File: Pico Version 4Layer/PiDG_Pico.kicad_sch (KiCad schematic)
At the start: 76 parts, among them J1 Conn_02x05_Odd_Even, J10 Trig, J11 Laser Enable, J12 Pixel Reset, J14 Pico Socket A, J15 Pico Socket B, J16 Laser En/PWM Trig/GND, J17 USB-C PD in, J2 Conn_02x05_Odd_Even, J3 Conn_02x05_Odd_Even, J4 Conn_02x05_Odd_Even, J5 Conn_02x05_Odd_Even, J6 Conn_02x05_Odd_Even, J7 Laser 1, J8 Laser 2, U1 74LVC1G04, U10 74AHCT1G08, U11 Raspberry Pi Pico 2 W, U12 74LVC1G17, U13 UCC27524, U14 CH224K, U15 AP63205WU, U16 LM66100, U17 LT3065EDD, U18 TPS3700DDC, U2 SN74LVC04AD, U3 74LVC1G04, U4 SN74LVC04AD, U5 74LVC1G04, U6 SN74LVC04AD, U7 74AHCT1G08, U8 74AHCT1G08, U9 NCP718xSN180

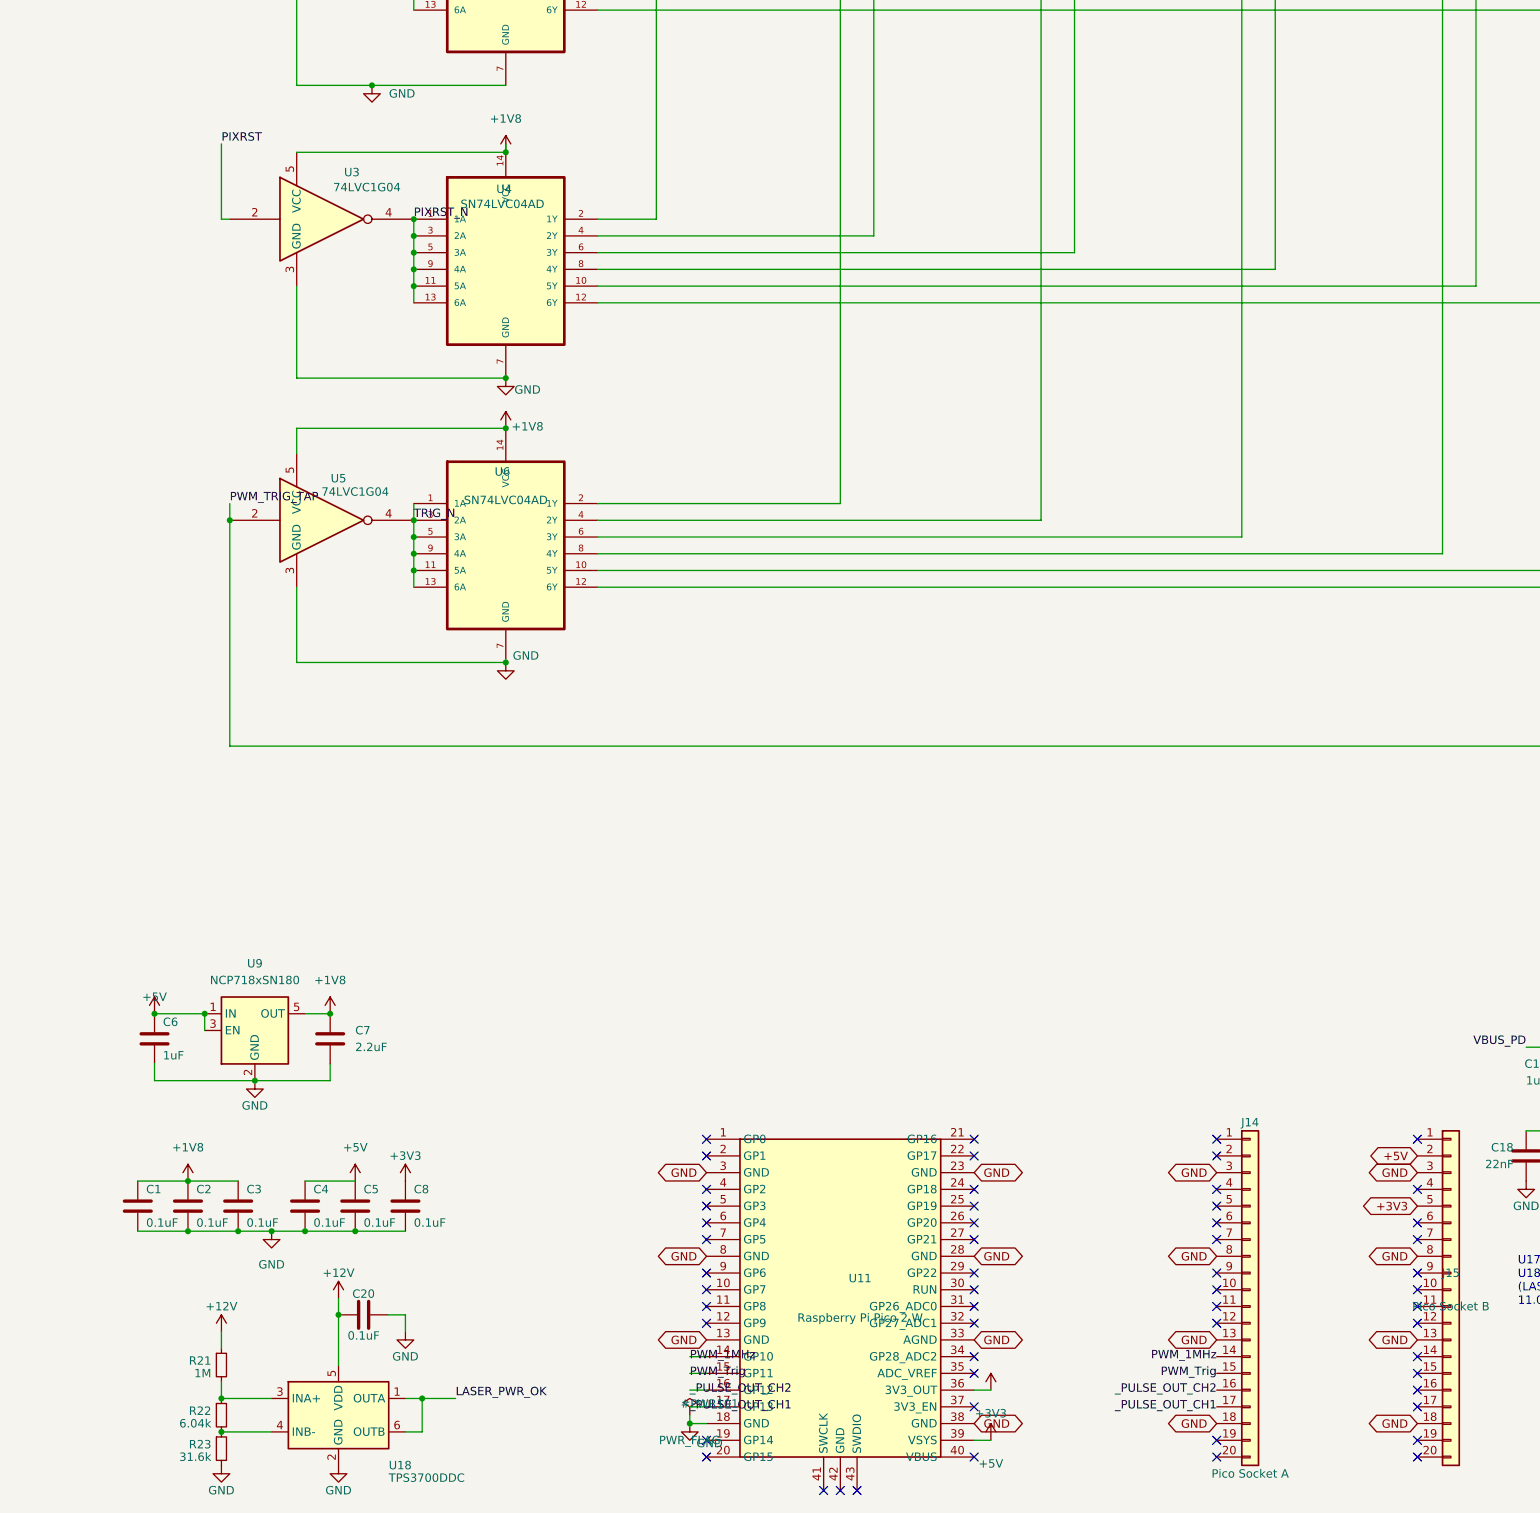
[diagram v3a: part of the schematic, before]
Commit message: Pixel-reset gate: optional camera pixel reset between pulse pairs
The Pico can now hold every camera's pixels in reset (TDRSTN low)
between pulse pairs, like a shutter, while the J12 BNC input keeps
working exactly as before.

Board
- U3 74LVC1G04 -> 74LVC1G00 (NAND, same SOT-23-5 footprint): through U4
  the cameras get TDRSTN = J12 input AND PIXRST_GATE, so either source
  resets the pixels.
- PIXRST_GATE = Pico GP16 (J15 pad 20) -> U3 pin 1 (previously NC), with
  R24 10k pull-up to +3V3 so the gate reads "no reset" unless driven low.
  Routed F.Cu from J15 pad 20, one B.Cu 45-degree hop, into U3 pad 1.
- ERC 0, DRC 0 / 0 unconnected, no real parity net conflicts; gerbers,
  drill, zip, CPLs and BOMs regenerated (U3 = SN74LVC1G00DBVR C7826;
  R24 joins the 10k line). 76 parts, 41 JLC lines.

Firmware
- PIXGATE 0|1|2 (off / while ARMED / always), PIXLEAD ns (pixels
  released this long before CH1, >= 5 cycles), PIXLAG ns (reset again
  this long after the last laser pulse). Validated on realized cycles:
  PIXLEAD + DELAY + WIDTH + PIXLAG <= 1/FREQ - 3 cycles.
- pio0 SM3 runs the existing pulse program on GP16 with the pad output
  inverted (GPIO_OVERRIDE_INVERT), enabled on the same cycle as CH1/CH2/
  MARKER; a stopped gate leaves the pixels free. SYNC moved to pio1 to
  free SM3 (the Pico 2 W's CYW43 driver takes pio2).
- STATUS reports PIXRESET (reset length per period, its start after CH1,
  and the free window); HELP documents the commands.
- tools/timing_check/check_pixgate.py: 1600 random sets against an
  exact model plus a cycle-level PIO simulation of CH1/CH2/gate
  (513 gated, 0 mismatches; mutation-tested). All existing checks give
  their unchanged expected counts. Strict-warning builds clean.

Docs: README (commands, PIXGATE section, STATUS, troubleshooting),
Hardware.md (pin map, pixel-reset chain, gate timing), JLC_ORDER.md.

Co-Authored-By: Claude Opus 5.5 (1M context) <noreply@anthropic.com>
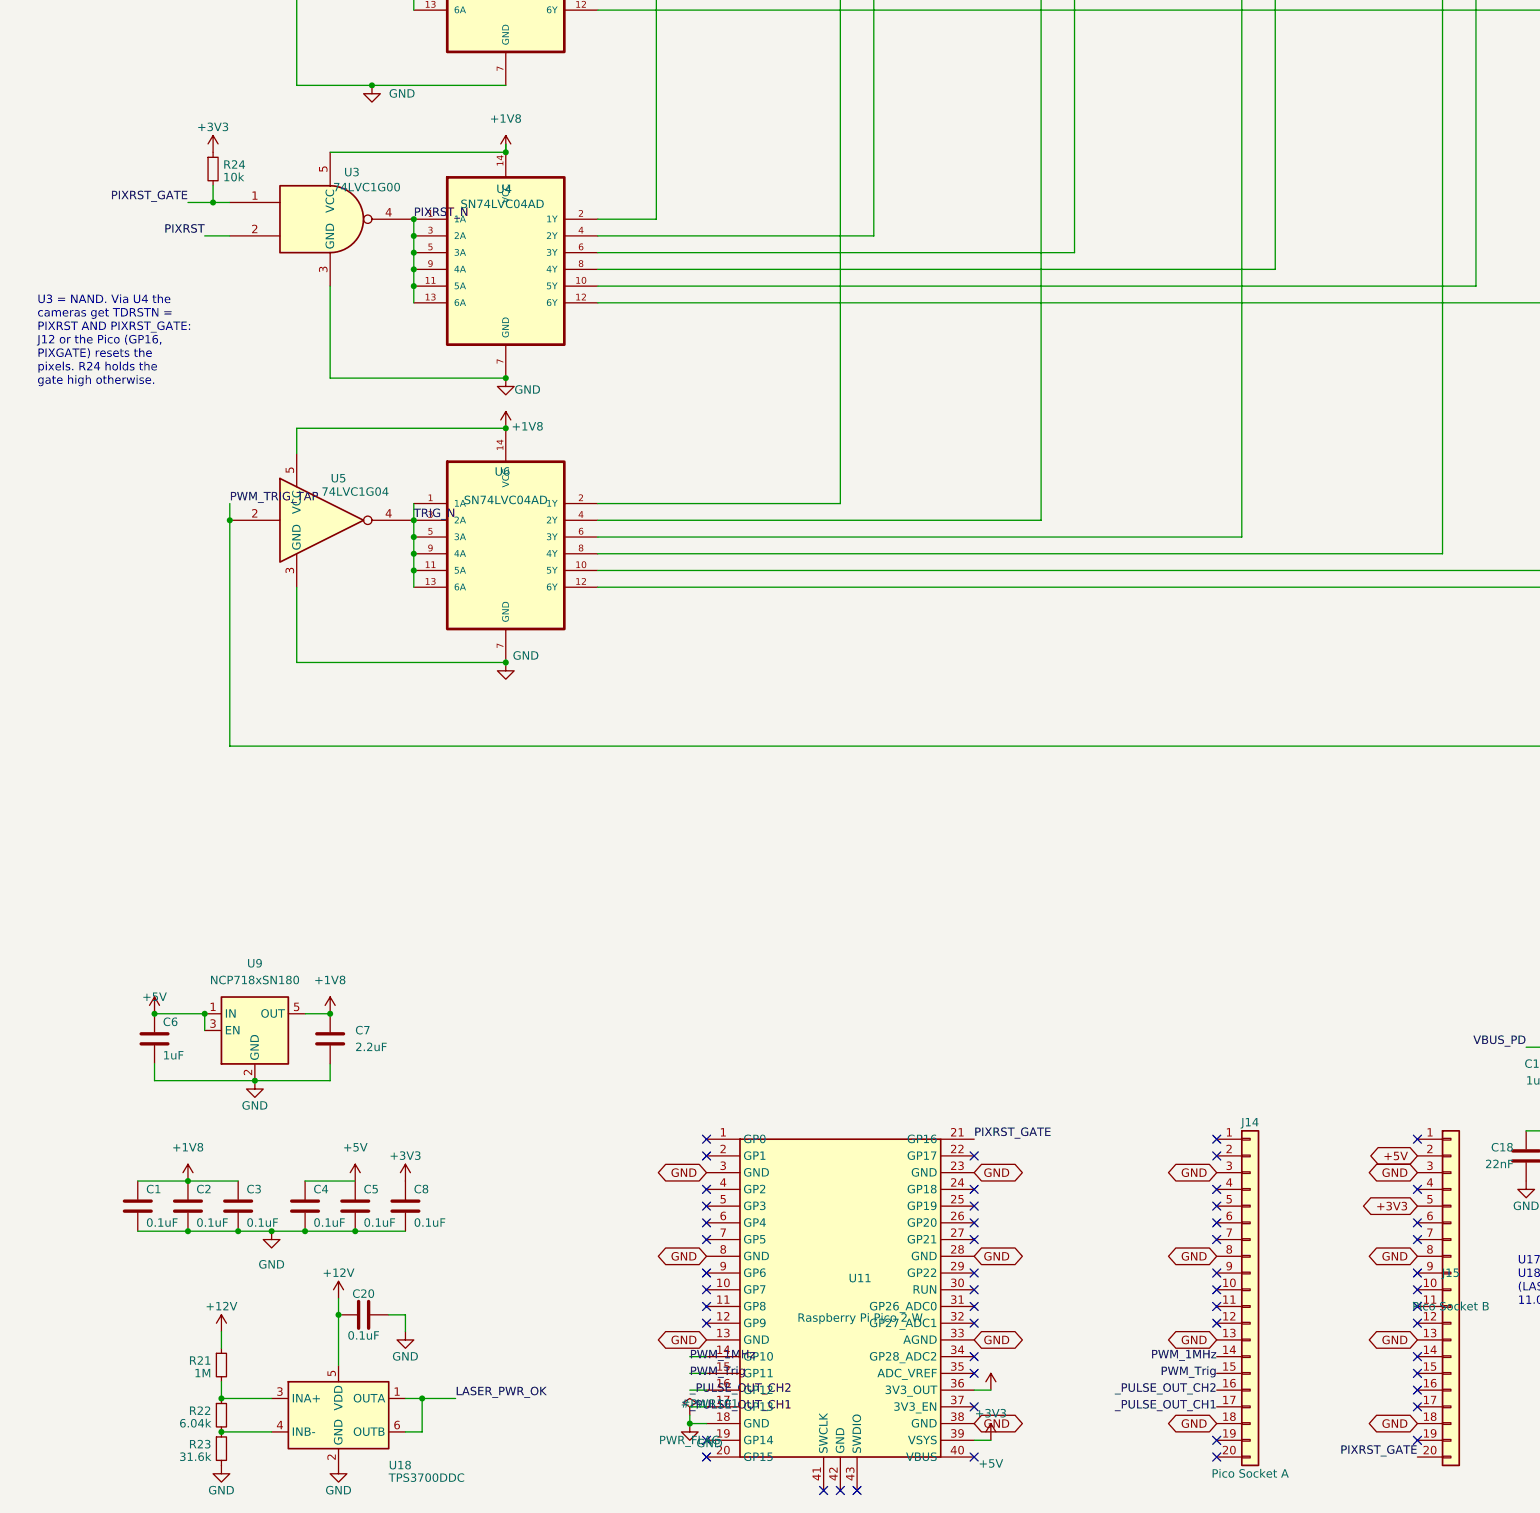
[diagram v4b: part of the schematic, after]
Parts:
- added R24: 10k, Resistor_SMD:R_0805_2012Metric_Pad1.20x1.40mm_HandSolder, symbol Device:R_Small
- U3: value 74LVC1G04 -> 74LVC1G00; symbol 74xGxx:74LVC1G04 -> 74xGxx:74LVC1G00
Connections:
- net +3V3: now also R24.1
- net PIXRST_GATE: now reaches U11.21 (GP16)
- net PIXRST_GATE: now also J15.20 (Pin_20), U3.1, R24.2
- no-connect marks 95 -> 93
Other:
- note added: "U3 = NAND. Via U4 the cameras get TDRSTN = PIXRST AND PIXRST_GATE: J12 or the Pico (GP16, PIXGATE) resets the pixels. R24 holds the gate high otherwise."
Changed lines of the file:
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@@
 	)
 	(no_connect
-		(at 157.48 227.33)
-	)
-	(no_connect
 		(at 340.36 172.72)
 	)
@@
 	)
 	(no_connect
-		(at 224.79 275.59)
-	)
-	(no_connect
 		(at 137.16 280.67)
 	)
@@
 	(wire
 		(pts
+			(xy 59.69 77.47) (xy 86.36 77.47)
+		)
+		(stroke
+			(width 0)
+			(type default)
+		)
+	)
+	(wire
+		(pts
+			(xy 59.69 97.79) (xy 59.69 111.76)
+		)
+		(stroke
+			(width 0)
+			(type default)
+		)
+	)
+	(wire
+		(pts
+			(xy 59.69 111.76) (xy 86.36 111.76)
+		)
+		(stroke
+			(width 0)
+			(type default)
+		)
+	)
+	(wire
+		(pts
+			(xy 40.64 90.17) (xy 44.45 90.17)
+		)
+		(stroke
+			(width 0)
+			(type default)
+		)
+	)
+	(label "PIXRST"
+		(at 40.64 90.17 0)
+		(effects
+			(font
+				(size 1.27 1.27)
+			)
+			(justify right bottom)
+		)
+	)
+	(wire
+		(pts
+			(xy 38.1 85.09) (xy 41.91 85.09)
+		)
+		(stroke
+			(width 0)
+			(type default)
+		)
+	)
+	(wire
+		(pts
+			(xy 41.91 85.09) (xy 44.45 85.09)
+		)
+		(stroke
+			(width 0)
+			(type default)
+		)
+	)
+	(junction
+		(at 41.91 85.09)
+		(diameter 0)
+		(color 0 0 0 0)
+	)
+	(label "PIXRST_GATE"
+		(at 38.1 85.09 0)
+		(effects
+			(font
+				(size 1.27 1.27)
+			)
+			(justify right bottom)
+		)
+	)
+	(wire
+		(pts
+			(xy 41.91 82.55) (xy 41.91 85.09)
+		)
+		(stroke
+			(width 0)
+			(type default)
+		)
+	)
+	(text "U3 = NAND. Via U4 the\ncameras get TDRSTN =\nPIXRST AND PIXRST_GATE:\nJ12 or the Pico (GP16,\nPIXGATE) resets the\npixels. R24 holds the\ngate high otherwise."
+		(exclude_from_sim no)
+		(at 15.24 113.03 0)
+		(effects
+			(font
+				(size 1.27 1.27)
+			)
+			(justify left bottom)
+		)
+	)
+	(label "PIXRST_GATE"
+		(at 224.79 275.59 0)
+		(effects
+			(font
+				(size 1.27 1.27)
+			)
+			(justify right bottom)
+		)
+	)
+	(label "PIXRST_GATE"
+		(at 157.48 227.33 0)
+		(effects
+			(font
+				(size 1.27 1.27)
+			)
+			(justify left bottom)
+		)
+	)
+	(wire
+		(pts
 			(xy 256.54 213.36) (xy 254 213.36)
 		)
@@
 	(wire
 		(pts
-			(xy 43.18 87.63) (xy 44.45 87.63)
-		)
-		(stroke
-			(width 0)
-			(type default)
-		)
-	)
-	(wire
-		(pts
 			(xy 54.61 67.31) (xy 66.04 67.31)
 		)
@@
 	(wire
 		(pts
-			(xy 54.61 97.79) (xy 54.61 111.76)
-		)
-		(stroke
-			(width 0)
-			(type default)
-		)
-	)
-	(wire
-		(pts
 			(xy 351.79 29.21) (xy 354.33 29.21)
 		)
@@
 	(wire
 		(pts
-			(xy 43.18 76.2) (xy 43.18 87.63)
-		)
-		(stroke
-			(width 0)
-			(type default)
-		)
-	)
-	(wire
-		(pts
 			(xy 236.22 31.75) (xy 236.22 53.34)
 		)
@@
 	(wire
 		(pts
-			(xy 54.61 111.76) (xy 86.36 111.76)
-		)
-		(stroke
-			(width 0)
-			(type default)
-		)
-	)
-	(wire
-		(pts
 			(xy 109.22 29.21) (xy 109.22 87.63)
 		)
@@
 	(wire
 		(pts
-			(xy 54.61 77.47) (xy 86.36 77.47)
-		)
-		(stroke
-			(width 0)
-			(type default)
-		)
-	)
-	(wire
-		(pts
 			(xy 205.74 31.75) (xy 205.74 50.8)
 		)
@@
 		)
 	)
-	(label "PIXRST"
-		(at 43.18 76.2 0)
-		(effects
-			(font
-				(size 1.27 1.27)
-			)
-			(justify left bottom)
-		)
-	)
 	(label "Sync3"
 		(at 176.53 31.75 0)
@@
 	)
 	(symbol
-		(lib_id "74xGxx:74LVC1G04")
+		(lib_id "74xGxx:74LVC1G00")
 		(at 59.69 87.63 0)
 		(unit 1)
@@
 			)
 		)
-		(property "Value" "74LVC1G04"
+		(property "Value" "74LVC1G00"
 			(at 65.278 82.804 0)
 			(show_name no)
@@
 			)
 		)
-		(property "Datasheet" "https://www.ti.com/lit/ds/symlink/sn74lvc1g04.pdf"
+		(property "Datasheet" "https://www.ti.com/lit/ds/symlink/sn74lvc1g00.pdf"
 			(at 59.69 87.63 0)
 			(hide yes)
@@
 			)
 		)
-		(property "Description" "Single NOT Gate, Low-Voltage CMOS"
+		(property "Description" "Pixel-reset combiner (1.8 V): NAND of PIXRST (J12 via U12) and PIXRST_GATE (Pico GP16); through U4 the cameras see TDRSTN = PIXRST AND GATE"
 			(at 59.69 87.63 0)
 			(hide yes)
@@
 					(unit 1)
 				)
+			)
+		)
+	)
+	(symbol
+		(lib_id "Device:R_Small")
+		(at 41.91 80.01 0)
+		(unit 1)
+		(body_style 1)
+		(exclude_from_sim no)
+		(in_bom yes)
+		(on_board yes)
+		(in_pos_files yes)
+		(dnp no)
+		(property "Reference" "R24"
+			(at 43.434 79.375 0)
+			(show_name no)
+			(do_not_autoplace no)
+			(effects
+				(font
+					(size 1.27 1.27)
+				)
+				(justify left)
+			)
+		)
+		(property "Value" "10k"
+			(at 43.434 81.28 0)
+			(show_name no)
+			(do_not_autoplace no)
+			(effects
+				(font
+					(size 1.27 1.27)
+				)
+				(justify left)
+			)
+		)
+		(property "Footprint" "Resistor_SMD:R_0805_2012Metric_Pad1.20x1.40mm_HandSolder"
+			(at 41.91 80.01 0)
+			(hide yes)
+			(show_name no)
+			(do_not_autoplace no)
+			(effects
+				(font
+					(size 1.27 1.27)
+				)
+			)
+		)
+		(property "Datasheet" ""
+			(at 41.91 80.01 0)
+			(hide yes)
+			(show_name no)
+			(do_not_autoplace no)
+			(effects
+				(font
+					(size 1.27 1.27)
+				)
+			)
+		)
+		(property "Description" "PIXRST_GATE pull-up: gate high (no pixel reset) unless the Pico drives it low"
+			(at 41.91 80.01 0)
+			(hide yes)
+			(show_name no)
+			(do_not_autoplace no)
+			(effects
+				(font
+					(size 1.27 1.27)
+				)
+			)
+		)
+		(pin "1"
+		)
+		(pin "2"
+		)
+		(instances
+			(project "PiDG_Pico"
+				(path "/e63e39d7-6ac0-4ffd-8aa3-1841a4541b55"
+					(reference "R24")
+					(unit 1)
+				)
+			)
+		)
+	)
+	(symbol
+		(lib_id "power:+3V3")
+		(at 41.91 77.47 0)
+		(unit 1)
+		(body_style 1)
+		(exclude_from_sim no)
+		(in_bom no)
+		(on_board no)
+		(in_pos_files no)
+		(dnp no)
+		(property "Reference" "#PWR154"
+			(at 41.91 71.12 0)
+			(hide yes)
+			(show_name no)
+			(do_not_autoplace no)
+			(effects
+				(font
+					(size 1.27 1.27)
+				)
+			)
+		)
+		(property "Value" "+3V3"
+			(at 41.91 73.66 0)
+			(show_name no)
+			(do_not_autoplace no)
+			(effects
+				(font
+					(size 1.27 1.27)
+				)
+			)
+		)
+		(property "Footprint" ""
+			(at 41.91 77.47 0)
+			(hide yes)
+			(show_name no)
+			(do_not_autoplace no)
+			(effects
+				(font
+					(size 1.27 1.27)
+				)
+			)
+		)
+		(property "Datasheet" ""
+			(at 41.91 77.47 0)
+			(hide yes)
+			(show_name no)
+			(do_not_autoplace no)
+			(effects
+				(font
+					(size 1.27 1.27)
+				)
+			)
+		)
+		(property "Description" "Power symbol creates a global label with name \"+3V3\""
+			(at 41.91 77.47 0)
+			(hide yes)
+			(show_name no)
+			(do_not_autoplace no)
+			(effects
+				(font
+					(size 1.27 1.27)
+				)
+			)
+		)
+		(pin "1"
+		)
+		(instances
+			(project "PiDG_Pico"
+				(path "/e63e39d7-6ac0-4ffd-8aa3-1841a4541b55"
+					(reference "#PWR154")
+					(unit 1)
+				)
